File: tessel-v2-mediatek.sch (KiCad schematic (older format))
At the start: 49 parts, among them U201 MT7620N, X201 20MHz

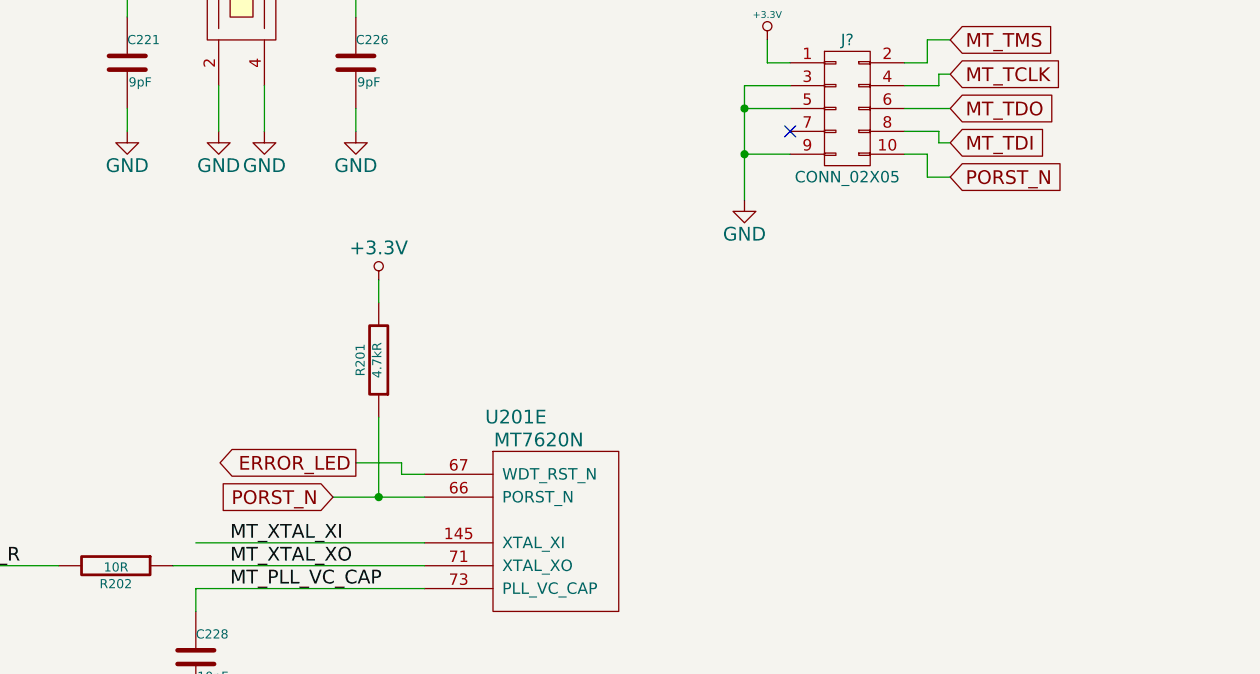
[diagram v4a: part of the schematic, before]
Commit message: still refactoring. usb is a pain
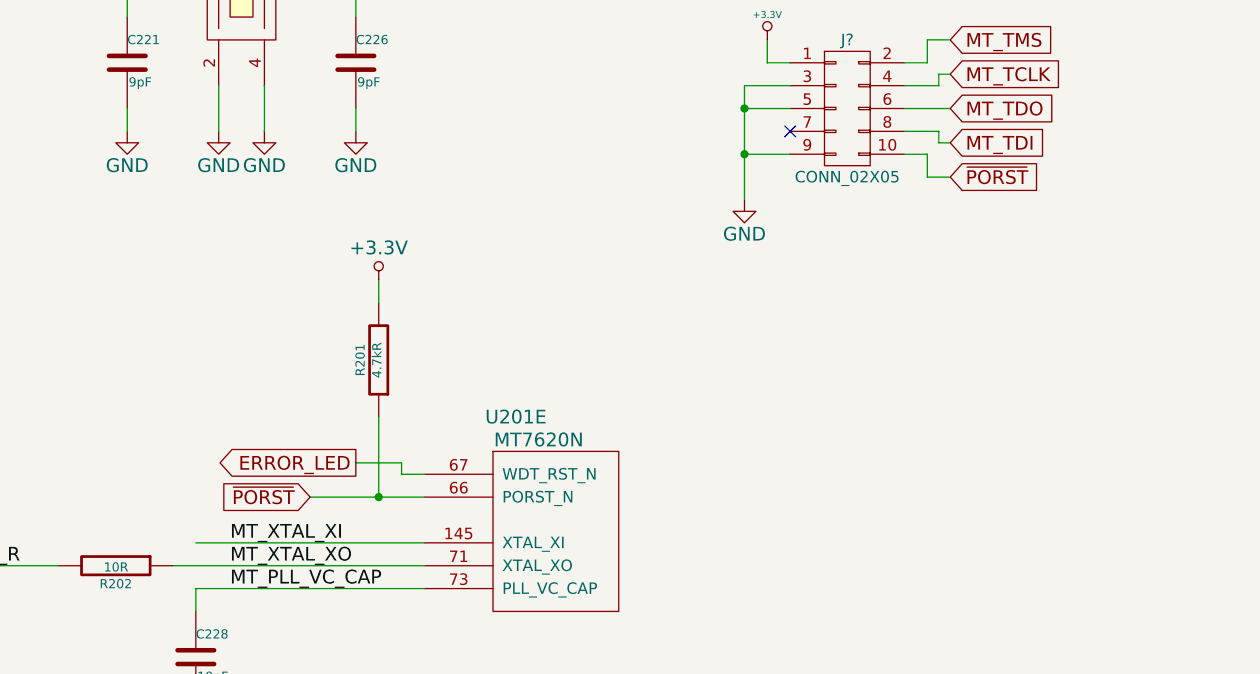
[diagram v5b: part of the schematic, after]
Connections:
- net labels added: ~PORST
- net labels removed: PORST_N
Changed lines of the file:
@@
 Text Label 1200 4300 0    60   ~ 0
 MT_XTAL_XO_R
-Text GLabel 3200 4000 0    60   Input ~ 0
-PORST_N
+Text GLabel 3100 4000 0    60   Input ~ 0
+~PORST
 $Comp
 L C C201
@@
 Connection ~ 3400 4000
 Wire Wire Line
-	3200 4000 3400 4000
+	3100 4000 3400 4000
 Wire Wire Line
 	3400 4000 3600 4000
@@
 	4000 6600 4000 6400
 Text GLabel 5900 2600 2    60   Input ~ 0
-PORST_N
+~PORST
 $Comp
 L CONN_02X05 J?

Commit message: last but not least: refactoring mediatek itself
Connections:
- wire segments 282 -> 248
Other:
- moved on the sheet: C201, C202, C203, C204, C205, C206, C207, C208, C209, C210, C211, C212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

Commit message: refactoring "complete"; verification begins...later
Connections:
- wire segments 248 -> 255
- no-connect marks 7 -> 5
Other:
- moved on the sheet: C201, C202, C203, C204, C205, C206, C207, C208, C209, C210, C211, C212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

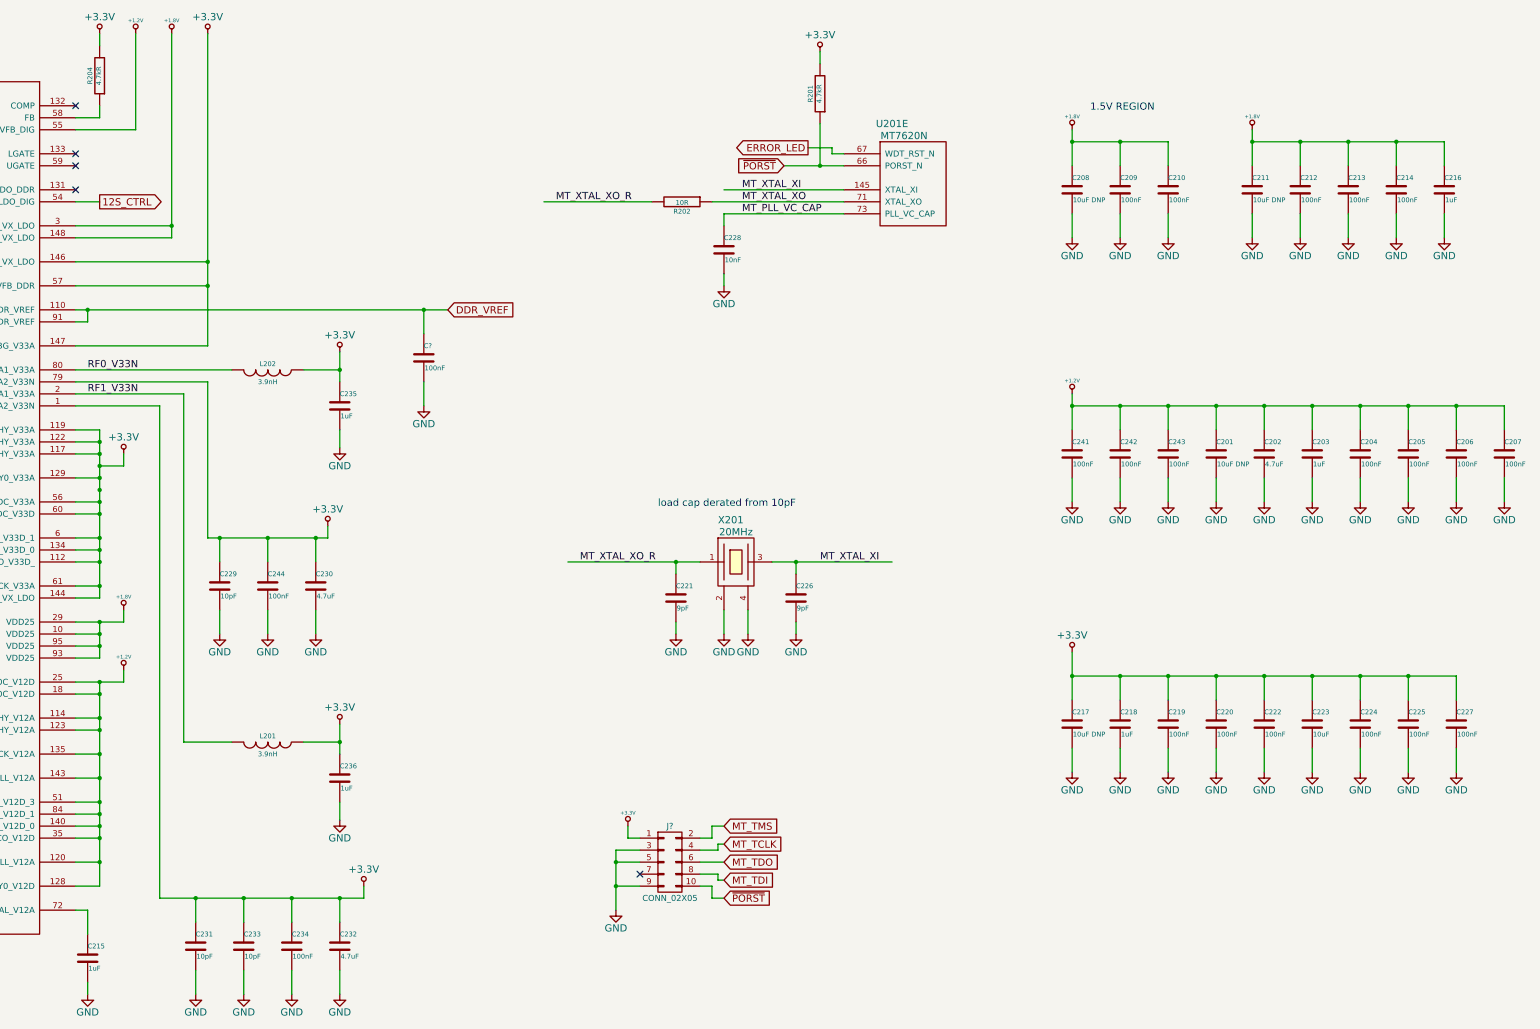
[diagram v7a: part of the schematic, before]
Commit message: reset annotation
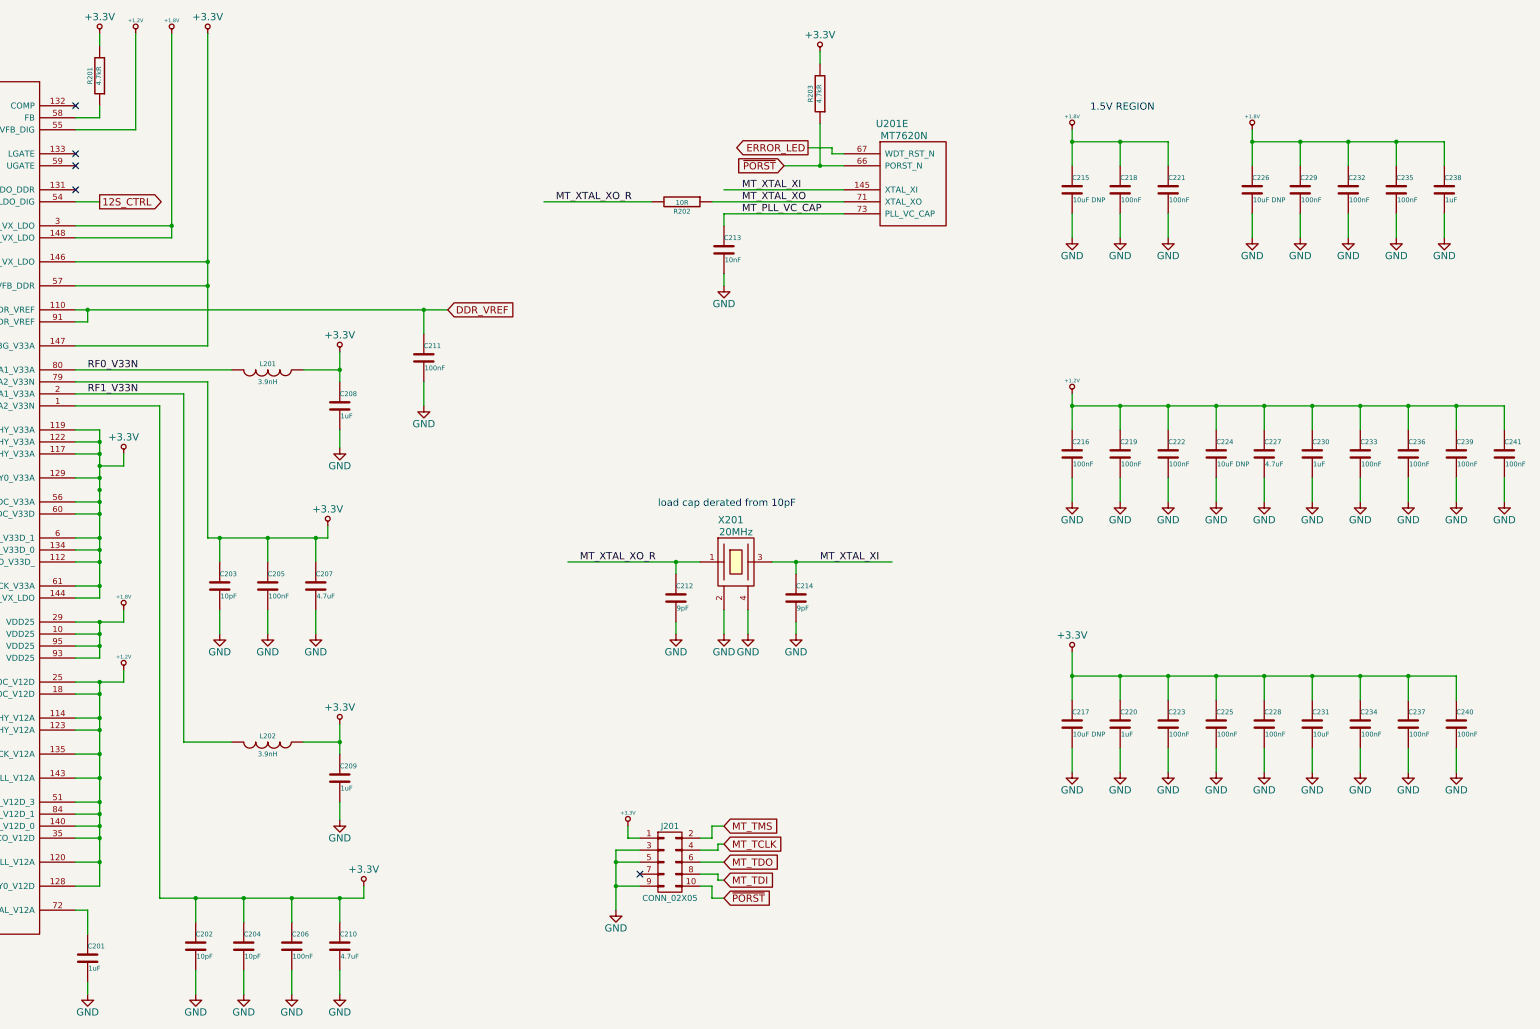
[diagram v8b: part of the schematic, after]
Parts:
- gave numbers to parts that had none: 2
- renumbered C215 to C201, C231 to C202, C229 to C203, C233 to C204, C244 to C205, C234 to C206, C230 to C207, C235 to C208, C236 to C209, C232 to C210, C221 to C212, C228 to C213, C226 to C214, C208 to C215, C241 to C216, C209 to C218, C242 to C219, C218 to C220, C210 to C221, C243 to C222, C219 to C223, C201 to C224, C220 to C225, C211 to C226, C202 to C227, C222 to C228, C212 to C229, C203 to C230, C223 to C231, C213 to C232, C204 to C233, C224 to C234, C214 to C235, C205 to C236, C225 to C237, C216 to C238, C206 to C239, C227 to C240, C207 to C241, L202 to L201, L201 to L202, R204 to R201, R201 to R203
